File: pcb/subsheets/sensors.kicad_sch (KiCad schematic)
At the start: 7 parts, among them U2 Barometer-KP212K1409XTMA1, U3 Thermometer-LM335D

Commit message: fixed everything (ERC is no longer mad)
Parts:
- removed R3, R4: 3k, symbol Device:R
- removed R5: 5.6k, symbol Device:R
- removed U3: Thermometer-LM335D, BeltFootprints:Thermometer-LM335D, symbol Thermometer-LM335D:Thermometer-LM335D
- added U3: AT30TS75A-SS8M, BeltFootprints:Thermometer-AT30TS75A-SS8M, symbol Thermometer-AT30TS75A-SS8M:Thermometer-AT30TS75A-SS8M
- U2: value Barometer-KP212K1409XTMA1 -> KP212K1409XTMA1
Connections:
- net +5V: now also U3.6 (A_{1}), U3.7 (A_{0}), U3.8 (V_{CC})
- net GND: now also U3.4 (GND), U3.5 (A_{2}); no longer U2.6 (GND_1), U2.8 (GND_2)
- net BaroVOut renamed V_{baro_raw}
- net DataBaro renamed V_{baro}
- new net GNDA: U2.6 (GND), U2.8 (GND)
- new net Thermo_SCL: U3.2 (SCL)
- new net Thermo_SDA: U3.1 (SDA)
- no-connect marks 5 -> 1
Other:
- note added: "Barometer outputs 0.5V < V_{raw} < 4.5V Pico I/O requires 0.3V < V_{ADC} < 3.0V V_{baro} = [R_{2} / (R_{1} + R_{2})] * V_{raw} V_{baro} = [10k / (5.6k + 10k)] * V_{raw} V_{baro} = 0.641 * V_{raw} min(V_{baro}) > min(V_{ADC}) 0.641 * min(V_{raw}) > min(V_{ADC}) 0.641 * 0.5V > 0.3V 0.321V > 0.3V max(V_{baro}) < max(V_{ADC}) 0.641 * max(V_{raw}) < max(V_{ADC}) 0.641 * 4.5V < 3.0V 2.88V < 3.0V"
- note added: "I2C address in binary, hex, and decimal: ADDR_{2} = 0b1001ZYX, with X=A_{0}, Y=A_{1}, Z=A_{2} ADDR_{16} = 0x48 + 0x4*A_{2} + 0x2*A_{1} + 0x1*A_{0} ADDR_{10} = 72 + 4A_{2} + 2A_{1} + 1A_{0} Values A_{0}=1, A_{1}=1, A_{2}=0 assigned arbitrarily. Chosen address is: 0b1001011 = 0x4B = 75."
- note added: "OUTPUT TYPE: Analog voltage"
- note added: "OUTPUT TYPE: I2C"
- note removed: "Barometer outputs 0.5V < BaroVOut < 4.5V Pico I/O requires 0.3V < VADC < 3.0V DataBaro = [R2 / (R1 + R2)] * BaroVOut = [10k / (5.6k + 10k)] * BaroVOut = 0.641 * BaroVOut min(DataBaro) > min(VADC) 0.641 * min(BaroVOut) > min(VADC) 0.641 * 0.5V > 0.3V 0.321V > 0.3V max(DataBaro) < max(VADC) 0.641 * max(BaroVOut) < max(VADC) 0.641 * 4.5V < 3.0V 2.88V < 3.0V"
- note removed: "Thermometer outputs 2.3V < TempVOut < 3.8V Pico I/O requires 0.3V < VADC < 3.0V DataTemp = [R5 / (R4 + R5)] * TempVOut = [5.6k / (3k + 5.6k)] * TempVOut = 0.651 * TempVOut min(DataTemp) > min(VADC) 0.651 * min(TempVOut) > min(VADC) 0.651 * 2.3V > 0.3V 1.50V > 0.3V max(DataTemp) < max(VADC) 0.651 * max(TempVOut) < max(VADC) 0.651 * 3.8V < 3.0V 2.47V < 3.0V"

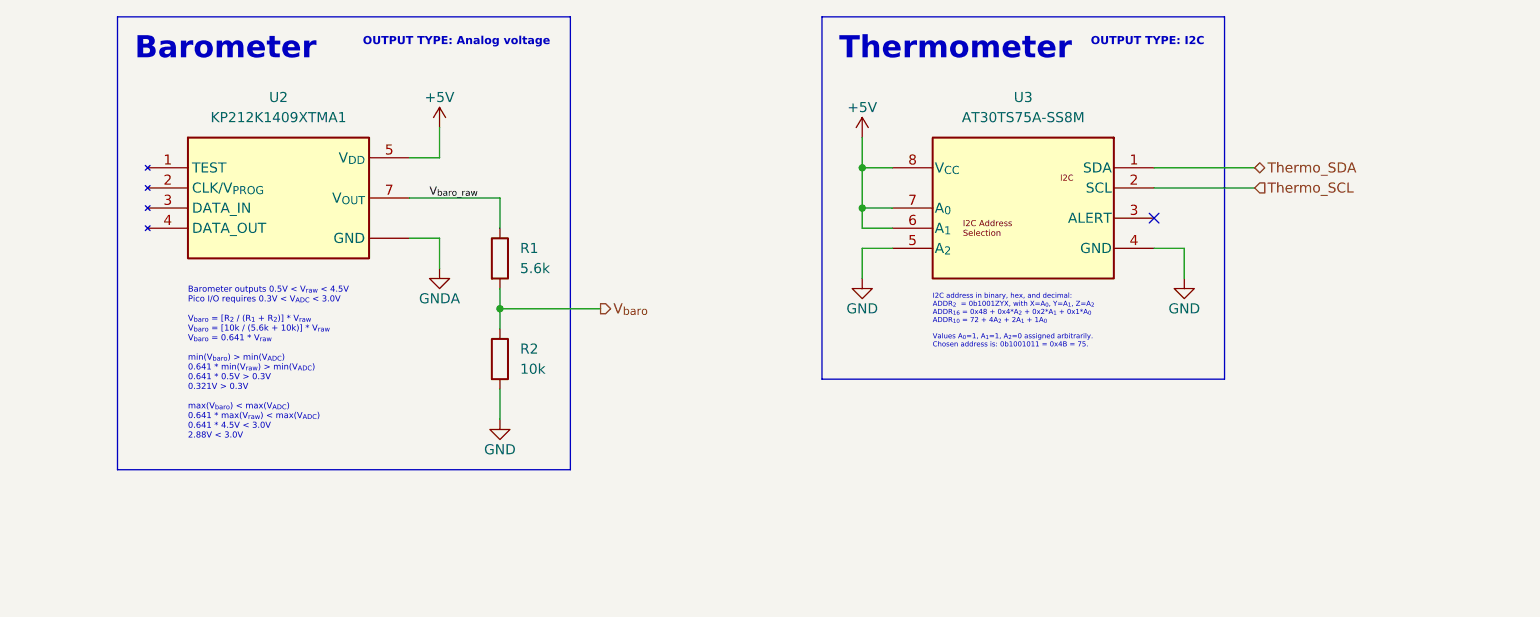
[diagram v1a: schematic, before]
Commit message: fixed all the resistors
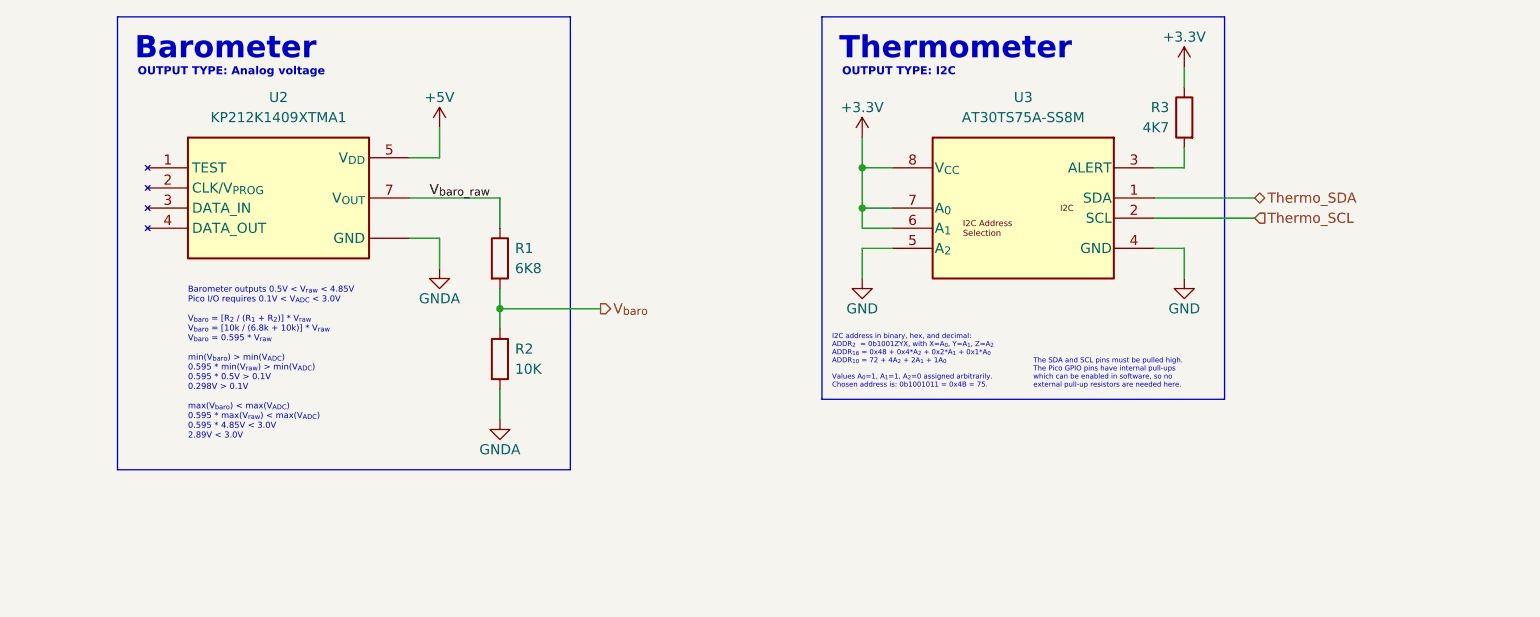
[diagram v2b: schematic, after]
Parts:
- added R3: 4K7, symbol Device:R
- R1: value 5.6k -> 6K8
- R2: value 10k -> 10K
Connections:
- net +5V: no longer U3.6 (A_{1}), U3.7 (A_{0}), U3.8 (V_{CC})
- net GND: no longer R2.2
- net GNDA: now also R2.2
- net at U3.3 (ALERT): now also R3.2
- new net +3.3V: R3.1, U3.6 (A_{1}), U3.7 (A_{0}), U3.8 (V_{CC})
- no-connect marks 1 -> 0
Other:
- note added: "Barometer outputs 0.5V < V_{raw} < 4.85V Pico I/O requires 0.1V < V_{ADC} < 3.0V V_{baro} = [R_{2} / (R_{1} + R_{2})] * V_{raw} V_{baro} = [10k / (6.8k + 10k)] * V_{raw} V_{baro} = 0.595 * V_{raw} min(V_{baro}) > min(V_{ADC}) 0.595 * min(V_{raw}) > min(V_{ADC}) 0.595 * 0.5V > 0.1V 0.298V > 0.1V max(V_{baro}) < max(V_{ADC}) 0.595 * max(V_{raw}) < max(V_{ADC}) 0.595 * 4.85V < 3.0V 2.89V < 3.0V"
- note added: "The SDA and SCL pins must be pulled high. The Pico GPIO pins have internal pull-ups which can be enabled in software, so no external pull-up resistors are needed here."
- note removed: "Barometer outputs 0.5V < V_{raw} < 4.5V Pico I/O requires 0.3V < V_{ADC} < 3.0V V_{baro} = [R_{2} / (R_{1} + R_{2})] * V_{raw} V_{baro} = [10k / (5.6k + 10k)] * V_{raw} V_{baro} = 0.641 * V_{raw} min(V_{baro}) > min(V_{ADC}) 0.641 * min(V_{raw}) > min(V_{ADC}) 0.641 * 0.5V > 0.3V 0.321V > 0.3V max(V_{baro}) < max(V_{ADC}) 0.641 * max(V_{raw}) < max(V_{ADC}) 0.641 * 4.5V < 3.0V 2.88V < 3.0V"
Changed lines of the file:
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@@
   (junction (at 157.48 74.93) (diameter 0) (color 0 0 0 0)
   )
-  (no_connect (at 194.31 76.2))
   (wire (pts (xy 104.14 64.77) (xy 104.14 68.58))
     (stroke (width 0) (type default))
@@
     (stroke (width 0) (type default))
   )
-  (wire (pts (xy 194.31 72.39) (xy 207.01 72.39))
+  (wire (pts (xy 194.31 76.2) (xy 207.01 76.2))
+    (stroke (width 0) (type default))
+  )
+  (wire (pts (xy 194.31 69.85) (xy 198.12 69.85))
     (stroke (width 0) (type default))
   )
@@
     (stroke (width 0) (type default))
   )
+  (wire (pts (xy 198.12 67.31) (xy 198.12 69.85))
+    (stroke (width 0) (type default))
+  )
   (wire (pts (xy 194.31 80.01) (xy 198.12 80.01))
     (stroke (width 0) (type default))
   )
+  (wire (pts (xy 198.12 57.15) (xy 198.12 59.69))
+    (stroke (width 0) (type default))
+  )
   (wire (pts (xy 104.14 78.74) (xy 104.14 82.55))
     (stroke (width 0) (type default))
@@
     (stroke (width 0) (type default))
   )
-  (wire (pts (xy 194.31 69.85) (xy 207.01 69.85))
+  (wire (pts (xy 194.31 73.66) (xy 207.01 73.66))
     (stroke (width 0) (type default))
   )
@@
   )
   (text_box "Thermometer"
-    (at 152.4 50.8 0) (size 50.8 45.72)
+    (at 152.4 50.8 0) (size 50.8 48.26)
     (stroke (width 0) (type default))
     (fill (type none))
@@
   )
   (text "I2C address in binary, hex, and decimal:\nADDR_{2}  = 0b1001ZYX, with X=A_{0}, Y=A_{1}, Z=A_{2}\nADDR_{16} = 0x48 + 0x4*A_{2} + 0x2*A_{1} + 0x1*A_{0}\nADDR_{10} = 72 + 4A_{2} + 2A_{1} + 1A_{0}\n\nValues A_{0}=1, A_{1}=1, A_{2}=0 assigned arbitrarily.\nChosen address is: 0b1001011 = 0x4B = 75."
-    (at 166.37 92.71 0)
+    (at 153.67 97.79 0)
     (effects (font (size 0.635 0.635)) (justify left bottom))
   )
-  (text "OUTPUT TYPE: I2C" (at 200.66 54.61 0)
-    (effects (font (size 1.016 1.016) bold) (justify right bottom))
-  )
-  (text "Barometer outputs 0.5V < V_{raw} < 4.5V\nPico I/O requires 0.3V < V_{ADC} < 3.0V\n\nV_{baro} = [R_{2} / (R_{1} + R_{2})] * V_{raw}\nV_{baro} = [10k / (5.6k + 10k)] * V_{raw}\nV_{baro} = 0.641 * V_{raw}\n\nmin(V_{baro}) > min(V_{ADC})\n0.641 * min(V_{raw}) > min(V_{ADC})\n0.641 * 0.5V > 0.3V\n0.321V > 0.3V\n\nmax(V_{baro}) < max(V_{ADC})\n0.641 * max(V_{raw}) < max(V_{ADC})\n0.641 * 4.5V < 3.0V\n2.88V < 3.0V\n\n\n"
+  (text "OUTPUT TYPE: I2C" (at 154.94 58.42 0)
+    (effects (font (size 1.016 1.016) bold) (justify left bottom))
+  )
+  (text "Barometer outputs 0.5V < V_{raw} < 4.85V\nPico I/O requires 0.1V < V_{ADC} < 3.0V\n\nV_{baro} = [R_{2} / (R_{1} + R_{2})] * V_{raw}\nV_{baro} = [10k / (6.8k + 10k)] * V_{raw}\nV_{baro} = 0.595 * V_{raw}\n\nmin(V_{baro}) > min(V_{ADC})\n0.595 * min(V_{raw}) > min(V_{ADC})\n0.595 * 0.5V > 0.1V\n0.298V > 0.1V\n\nmax(V_{baro}) < max(V_{ADC})\n0.595 * max(V_{raw}) < max(V_{ADC})\n0.595 * 4.85V < 3.0V\n2.89V < 3.0V\n\n\n"
     (at 72.39 106.68 0)
     (effects (font (size 0.762 0.762)) (justify left bottom))
   )
-  (text "OUTPUT TYPE: Analog voltage" (at 118.11 54.61 0)
-    (effects (font (size 1.016 1.016) (thickness 0.2032) bold) (justify right bottom))
+  (text "The SDA and SCL pins must be pulled high.\nThe Pico GPIO pins have internal pull-ups\nwhich can be enabled in software, so no\nexternal pull-up resistors are needed here."
+    (at 179.07 97.79 0)
+    (effects (font (size 0.635 0.635)) (justify left bottom))
+  )
+  (text "OUTPUT TYPE: Analog voltage" (at 66.04 58.42 0)
+    (effects (font (size 1.016 1.016) (thickness 0.2032) bold) (justify left bottom))
   )
   (label "V_{baro_raw}" (at 102.87 73.66 0) (fields_autoplaced)
-    (effects (font (size 1.016 1.016)) (justify left bottom))
+    (effects (font (size 1.27 1.27)) (justify left bottom))
   )
   (hierarchical_label "V_{baro}" (shape output) (at 124.46 87.63 0) (fields_autoplaced)
     (effects (font (size 1.27 1.27)) (justify left))
   )
-  (hierarchical_label "Thermo_SDA" (shape bidirectional) (at 207.01 69.85 0) (fields_autoplaced)
+  (hierarchical_label "Thermo_SDA" (shape bidirectional) (at 207.01 73.66 0) (fields_autoplaced)
     (effects (font (size 1.27 1.27)) (justify left))
   )
-  (hierarchical_label "Thermo_SCL" (shape input) (at 207.01 72.39 0) (fields_autoplaced)
+  (hierarchical_label "Thermo_SCL" (shape input) (at 207.01 76.2 0) (fields_autoplaced)
     (effects (font (size 1.27 1.27)) (justify left))
   )
@@
     )
   )
-  (symbol (lib_id "power:+5V") (at 157.48 66.04 0) (mirror y) (unit 1)
+  (symbol (lib_id "Device:R") (at 198.12 63.5 0) (mirror y) (unit 1)
+    (in_bom yes) (on_board yes) (dnp no)
+    (property "Reference" "R3" (at 196.215 62.23 0)
+      (effects (font (size 1.27 1.27)) (justify left))
+    )
+    (property "Value" "4K7" (at 196.215 64.77 0)
+      (effects (font (size 1.27 1.27)) (justify left))
+    )
+    (property "Footprint" "" (at 199.898 63.5 90)
+      (effects (font (size 1.27 1.27)) hide)
+    )
+    (property "Datasheet" "~" (at 198.12 63.5 0)
+      (effects (font (size 1.27 1.27)) hide)
+    )
+    (pin "1")
+    (pin "2")
+    (instances
+      (project "belt"
+        (path "/33e5c18d-f516-4ab7-aaea-c68685305111/74e42d83-2281-4435-b501-ae78499fc404"
+          (reference "R3") (unit 1)
+        )
+      )
+    )
+  )
+  (symbol (lib_id "power:+3.3V") (at 157.48 66.04 0) (unit 1)
     (in_bom yes) (on_board yes) (dnp no)
     (property "Reference" "#PWR010" (at 157.48 69.85 0)
       (effects (font (size 1.27 1.27)) hide)
     )
-    (property "Value" "+5V" (at 157.48 62.23 0)
+    (property "Value" "+3.3V" (at 157.48 62.23 0)
       (effects (font (size 1.27 1.27)))
     )
@@
     )
   )
-  (symbol (lib_id "power:GND") (at 111.76 101.6 0) (unit 1)
+  (symbol (lib_id "power:GNDA") (at 111.76 101.6 0) (unit 1)
     (in_bom yes) (on_board yes) (dnp no)
     (property "Reference" "#PWR09" (at 111.76 107.95 0)
       (effects (font (size 1.27 1.27)) hide)
     )
-    (property "Value" "GND" (at 111.76 105.41 0)
+    (property "Value" "GNDA" (at 111.76 105.41 0)
       (effects (font (size 1.27 1.27)))
     )
@@
     )
   )
+  (symbol (lib_id "power:+3.3V") (at 198.12 57.15 0) (unit 1)
+    (in_bom yes) (on_board yes) (dnp no)
+    (property "Reference" "#PWR012" (at 198.12 60.96 0)
+      (effects (font (size 1.27 1.27)) hide)
+    )
+    (property "Value" "+3.3V" (at 198.12 53.34 0)
+      (effects (font (size 1.27 1.27)))
+    )
+    (property "Footprint" "" (at 198.12 57.15 0)
+      (effects (font (size 1.27 1.27)) hide)
+    )
+    (property "Datasheet" "" (at 198.12 57.15 0)
+      (effects (font (size 1.27 1.27)) hide)
+    )
+    (pin "1")
+    (instances
+      (project "belt"
+        (path "/33e5c18d-f516-4ab7-aaea-c68685305111/74e42d83-2281-4435-b501-ae78499fc404"
+          (reference "#PWR012") (unit 1)
+        )
+      )
+    )
+  )
   (symbol (lib_id "Device:R") (at 111.76 81.28 0) (unit 1)
-    (in_bom yes) (on_board yes) (dnp no) (fields_autoplaced)
-    (property "Reference" "R1" (at 114.3 80.01 0)
-      (effects (font (size 1.27 1.27)) (justify left))
-    )
-    (property "Value" "5.6k" (at 114.3 82.55 0)
+    (in_bom yes) (on_board yes) (dnp no)
+    (property "Reference" "R1" (at 113.665 80.01 0)
+      (effects (font (size 1.27 1.27)) (justify left))
+    )
+    (property "Value" "6K8" (at 113.665 82.55 0)
       (effects (font (size 1.27 1.27)) (justify left))
     )
@@
   )
   (symbol (lib_id "Device:R") (at 111.76 93.98 0) (unit 1)
-    (in_bom yes) (on_board yes) (dnp no) (fields_autoplaced)
-    (property "Reference" "R2" (at 114.3 92.71 0)
-      (effects (font (size 1.27 1.27)) (justify left))
-    )
-    (property "Value" "10k" (at 114.3 95.25 0)
+    (in_bom yes) (on_board yes) (dnp no)
+    (property "Reference" "R2" (at 113.665 92.71 0)
+      (effects (font (size 1.27 1.27)) (justify left))
+    )
+    (property "Value" "10K" (at 113.665 95.25 0)
       (effects (font (size 1.27 1.27)) (justify left))
     )
@@
   (symbol (lib_id "power:GND") (at 198.12 83.82 0) (mirror y) (unit 1)
     (in_bom yes) (on_board yes) (dnp no)
-    (property "Reference" "#PWR012" (at 198.12 90.17 0)
+    (property "Reference" "#PWR013" (at 198.12 90.17 0)
       (effects (font (size 1.27 1.27)) hide)
     )
@@
       (project "belt"
         (path "/33e5c18d-f516-4ab7-aaea-c68685305111/74e42d83-2281-4435-b501-ae78499fc404"
-          (reference "#PWR012") (unit 1)
-        )
-      )
+          (reference "#PWR013") (unit 1)
+        )
+      )

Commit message: mostly finished schematic
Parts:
- added C1, C2: 100n, symbol Device:C
- added C3: 10n, symbol Device:C
- added R3: 33K, symbol Device:R
- renumbered R3 to R4
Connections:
- net +3.3V: now also C3.2
- net +5V: now also C1.1
- net GND: now also C3.1
- net GNDA: now also C1.2, C2.2
- net V_{baro}: now also C2.1, R3.1; no longer R1.2, R2.1
- new net: R1.2, R2.1, R3.2
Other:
- note removed: "Barometer outputs 0.5V < V_{raw} < 4.85V Pico I/O requires 0.1V < V_{ADC} < 3.0V V_{baro} = [R_{2} / (R_{1} + R_{2})] * V_{raw} V_{baro} = [10k / (6.8k + 10k)] * V_{raw} V_{baro} = 0.595 * V_{raw} min(V_{baro}) > min(V_{ADC}) 0.595 * min(V_{raw}) > min(V_{ADC}) 0.595 * 0.5V > 0.1V 0.298V > 0.1V max(V_{baro}) < max(V_{ADC}) 0.595 * max(V_{raw}) < max(V_{ADC}) 0.595 * 4.85V < 3.0V 2.89V < 3.0V"
- note removed: "I2C address in binary, hex, and decimal: ADDR_{2} = 0b1001ZYX, with X=A_{0}, Y=A_{1}, Z=A_{2} ADDR_{16} = 0x48 + 0x4*A_{2} + 0x2*A_{1} + 0x1*A_{0} ADDR_{10} = 72 + 4A_{2} + 2A_{1} + 1A_{0} Values A_{0}=1, A_{1}=1, A_{2}=0 assigned arbitrarily. Chosen address is: 0b1001011 = 0x4B = 75."
- note removed: "The SDA and SCL pins must be pulled high. The Pico GPIO pins have internal pull-ups which can be enabled in software, so no external pull-up resistors are needed here."
- moved on the sheet: R1, R2, R4, U2, U3

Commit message: finished schematic v0.3
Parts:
- renumbered R1 to R3, R2 to R4, R3 to R5, R4 to R6
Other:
- moved on the sheet: C1, C2, C3, R3, R4, R5, R6, U2, U3

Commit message: modified footprints
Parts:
- C1, C2, C3: footprint (none) -> Capacitor_SMD:C_1206_3216Metric_Pad1.33x1.80mm_HandSolder
- R3, R4, R5, R6: footprint (none) -> Resistor_THT:R_Axial_DIN0207_L6.3mm_D2.5mm_P10.16mm_Horizontal
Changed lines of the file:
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@@
       (effects (font (size 1.27 1.27)) (justify left))
     )
-    (property "Footprint" "" (at 218.948 76.2 90)
+    (property "Footprint" "Resistor_THT:R_Axial_DIN0207_L6.3mm_D2.5mm_P10.16mm_Horizontal" (at 218.948 76.2 90)
       (effects (font (size 1.27 1.27)) hide)
     )
@@
       (effects (font (size 1.27 1.27)))
     )
-    (property "Footprint" "" (at 102.87 76.5048 0)
+    (property "Footprint" "Capacitor_SMD:C_1206_3216Metric_Pad1.33x1.80mm_HandSolder" (at 102.87 76.5048 0)
       (effects (font (size 1.27 1.27)) hide)
     )
@@
       (effects (font (size 1.27 1.27)) (justify left))
     )
-    (property "Footprint" "" (at 114.6048 114.3 0)
+    (property "Footprint" "Capacitor_SMD:C_1206_3216Metric_Pad1.33x1.80mm_HandSolder" (at 114.6048 114.3 0)
       (effects (font (size 1.27 1.27)) hide)
     )
@@
       (effects (font (size 1.27 1.27)) (justify left))
     )
-    (property "Footprint" "" (at 102.108 95.25 90)
+    (property "Footprint" "Resistor_THT:R_Axial_DIN0207_L6.3mm_D2.5mm_P10.16mm_Horizontal" (at 102.108 95.25 90)
       (effects (font (size 1.27 1.27)) hide)
     )
@@
       (effects (font (size 1.27 1.27)) (justify left))
     )
-    (property "Footprint" "" (at 102.108 110.49 90)
+    (property "Footprint" "Resistor_THT:R_Axial_DIN0207_L6.3mm_D2.5mm_P10.16mm_Horizontal" (at 102.108 110.49 90)
       (effects (font (size 1.27 1.27)) hide)
     )
@@
       (effects (font (size 1.27 1.27)) (justify right))
     )
-    (property "Footprint" "" (at 173.6852 83.82 0)
+    (property "Footprint" "Capacitor_SMD:C_1206_3216Metric_Pad1.33x1.80mm_HandSolder" (at 173.6852 83.82 0)
       (effects (font (size 1.27 1.27)) hide)
     )
@@
       (effects (font (size 1.27 1.27)))
     )
-    (property "Footprint" "" (at 107.95 101.092 90)
-      (effects (font (size 1.27 1.27)) hide)
-    )
+    (property "Footprint" "Resistor_THT:R_Axial_DIN0207_L6.3mm_D2.5mm_P10.16mm_Horizontal" (at 107.95 101.092 90)
+      (effects (font (size 1.27 1.27)) hide)
+    )
